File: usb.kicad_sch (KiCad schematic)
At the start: 5 parts, among them U7 USBLC6-2P6

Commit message: added diode
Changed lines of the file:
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@@
 		(color 0 0 0 0)
 	)
+	(junction
+		(at 27.94 111.76)
+		(diameter 0)
+		(color 0 0 0 0)
+	)
 	(wire
 		(pts
@@
 	(wire
 		(pts
+			(xy 27.94 111.76) (xy 27.94 113.03)
+		)
+		(stroke
+			(width 0)
+			(type default)
+		)
+	)
+	(wire
+		(pts
 			(xy 39.37 106.68) (xy 39.37 111.76)
 		)
@@
 	(wire
 		(pts
+			(xy 24.13 111.76) (xy 27.94 111.76)
+		)
+		(stroke
+			(width 0)
+			(type default)
+		)
+	)
+	(wire
+		(pts
 			(xy 27.94 68.58) (xy 31.75 68.58)
 		)
@@
 	(wire
 		(pts
-			(xy 27.94 106.68) (xy 27.94 113.03)
+			(xy 27.94 106.68) (xy 27.94 111.76)
 		)
 		(stroke
@@
 			)
 		)
+	)
+	(symbol
+		(lib_id "power:PWR_FLAG")
+		(at 24.13 111.76 0)
+		(unit 1)
+		(exclude_from_sim no)
+		(in_bom yes)
+		(on_board yes)
+		(dnp no)
+		(fields_autoplaced yes)
+		(property "Reference" "#FLG02"
+			(at 24.13 109.855 0)
+			(effects
+				(font
+					(size 1.27 1.27)
+				)
+				(hide yes)
+			)
+		)
+		(property "Value" "PWR_FLAG"
+			(at 24.13 106.68 0)
+			(effects
+				(font
+					(size 1.27 1.27)
+				)
+			)
+		)
+		(property "Footprint" ""
+			(at 24.13 111.76 0)
+			(effects
+				(font
+					(size 1.27 1.27)
+				)
+				(hide yes)
+			)
+		)
+		(property "Datasheet" "~"
+			(at 24.13 111.76 0)
+			(effects
+				(font
+					(size 1.27 1.27)
+				)
+				(hide yes)
+			)
+		)
+		(property "Description" "Special symbol for telling ERC where power comes from"
+			(at 24.13 111.76 0)
+			(effects
+				(font
+					(size 1.27 1.27)
+				)
+				(hide yes)
+			)
+		)
+		(pin "1"
+		)
+		(instances
+			(project ""
+				(path "/84b8b555-aaa5-476b-b0f2-2d0f894bf0e6/4cda7d87-7e9e-45c2-9c67-fc3e262886b2"
+					(reference "#FLG02")
+					(unit 1)
+				)
+			)
+		)

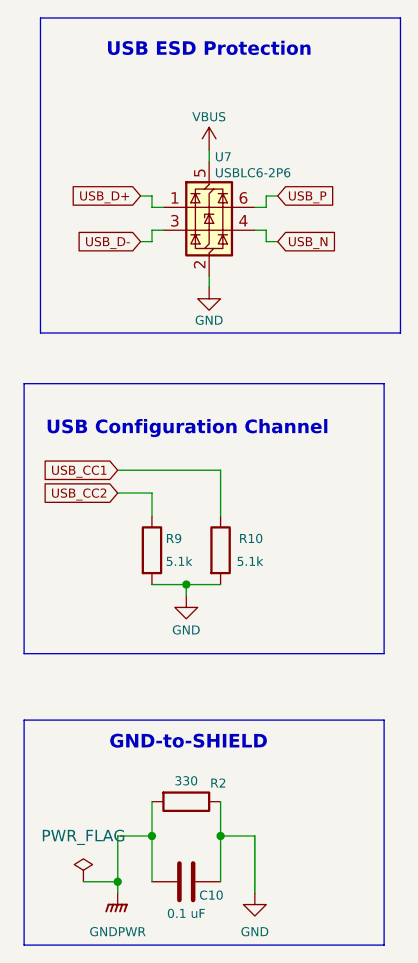
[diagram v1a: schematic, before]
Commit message: separated voltage source labels
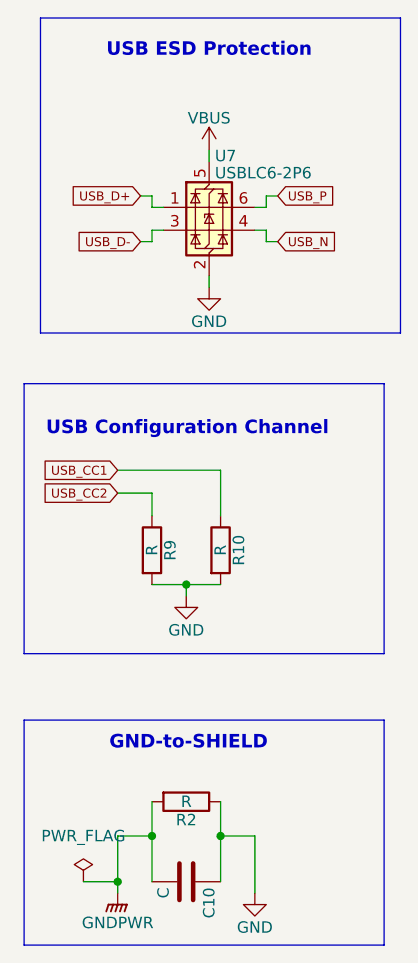
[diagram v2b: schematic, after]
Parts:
- C10: value 0.1 uF -> C
- R10, R9: value 5.1k -> R
- R2: value 330 -> R
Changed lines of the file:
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@@
 		(dnp no)
 		(fields_autoplaced yes)
-		(property "Reference" "#FLG02"
+		(property "Reference" "#FLG2"
 			(at 24.13 109.855 0)
 			(effects
@@
 			(project ""
 				(path "/84b8b555-aaa5-476b-b0f2-2d0f894bf0e6/4cda7d87-7e9e-45c2-9c67-fc3e262886b2"
-					(reference "#FLG02")
+					(reference "#FLG2")
 					(unit 1)
 				)
@@
 		(on_board yes)
 		(dnp no)
-		(property "Reference" "#PWR05"
+		(property "Reference" "#PWR5"
 			(at 27.94 118.11 0)
 			(effects
@@
 		)
 		(property "Value" "GNDPWR"
-			(at 27.94 117.348 0)
-			(effects
-				(font
-					(size 1 1)
+			(at 27.94 116.332 0)
+			(effects
+				(font
+					(size 1.27 1.27)
 				)
 			)
@@
 			(project "apex"
 				(path "/84b8b555-aaa5-476b-b0f2-2d0f894bf0e6/4cda7d87-7e9e-45c2-9c67-fc3e262886b2"
-					(reference "#PWR05")
+					(reference "#PWR5")
 					(unit 1)
 				)
@@
 		(on_board yes)
 		(dnp no)
-		(property "Reference" "#PWR013"
+		(property "Reference" "#PWR13"
 			(at 35.56 86.36 0)
 			(effects
@@
 			(effects
 				(font
-					(size 1 1)
+					(size 1.27 1.27)
 				)
 			)
@@
 			(project "apex"
 				(path "/84b8b555-aaa5-476b-b0f2-2d0f894bf0e6/4cda7d87-7e9e-45c2-9c67-fc3e262886b2"
-					(reference "#PWR013")
+					(reference "#PWR13")
 					(unit 1)
 				)
@@
 		(on_board yes)
 		(dnp no)
-		(property "Reference" "#PWR015"
+		(property "Reference" "#PWR15"
 			(at 43.18 119.38 0)
 			(effects
@@
 		)
 		(property "Value" "GND"
-			(at 43.18 117.348 0)
-			(effects
-				(font
-					(size 1 1)
+			(at 43.18 116.84 0)
+			(effects
+				(font
+					(size 1.27 1.27)
 				)
 			)
@@
 			(project "apex"
 				(path "/84b8b555-aaa5-476b-b0f2-2d0f894bf0e6/4cda7d87-7e9e-45c2-9c67-fc3e262886b2"
-					(reference "#PWR015")
+					(reference "#PWR15")
 					(unit 1)
 				)
@@
 		(dnp no)
 		(property "Reference" "R9"
-			(at 33.274 73.66 0)
-			(effects
-				(font
-					(size 1 1)
-				)
-				(justify left)
-			)
-		)
-		(property "Value" "5.1k"
-			(at 33.274 76.2 0)
-			(effects
-				(font
-					(size 1 1)
-				)
-				(justify left)
+			(at 33.782 74.93 90)
+			(effects
+				(font
+					(size 1.27 1.27)
+				)
+			)
+		)
+		(property "Value" "R"
+			(at 31.75 74.93 90)
+			(effects
+				(font
+					(size 1.27 1.27)
+				)
 			)
 		)
@@
 		(dnp no)
 		(property "Reference" "R2"
-			(at 39.116 100.838 90)
-			(effects
-				(font
-					(size 1 1)
-				)
-			)
-		)
-		(property "Value" "330"
-			(at 35.56 100.584 90)
-			(effects
-				(font
-					(size 1 1)
+			(at 35.56 104.902 90)
+			(effects
+				(font
+					(size 1.27 1.27)
+				)
+			)
+		)
+		(property "Value" "R"
+			(at 35.56 102.87 90)
+			(effects
+				(font
+					(size 1.27 1.27)
 				)
 			)
@@
 		(on_board yes)
 		(dnp no)
-		(property "Reference" "#PWR036"
+		(property "Reference" "#PWR36"
 			(at 38.1 52.07 0)
 			(effects
@@
 		)
 		(property "Value" "GND"
-			(at 38.1 49.403 0)
-			(effects
-				(font
-					(size 1 1)
+			(at 38.1 49.53 0)
+			(effects
+				(font
+					(size 1.27 1.27)
 				)
 			)
@@
 			(project "apex"
 				(path "/84b8b555-aaa5-476b-b0f2-2d0f894bf0e6/4cda7d87-7e9e-45c2-9c67-fc3e262886b2"
-					(reference "#PWR036")
+					(reference "#PWR36")
 					(unit 1)
 				)
@@
 		(on_board yes)
 		(dnp no)
-		(property "Reference" "#PWR035"
+		(property "Reference" "#PWR35"
 			(at 38.1 34.29 0)
 			(effects
@@
 		)
 		(property "Value" "VBUS"
-			(at 38.1 26.797 0)
-			(effects
-				(font
-					(size 1 1)
+			(at 38.1 26.924 0)
+			(effects
+				(font
+					(size 1.27 1.27)
 				)
 			)
@@
 			(project "apex"
 				(path "/84b8b555-aaa5-476b-b0f2-2d0f894bf0e6/4cda7d87-7e9e-45c2-9c67-fc3e262886b2"
-					(reference "#PWR035")
+					(reference "#PWR35")
 					(unit 1)
 				)
@@
 		(dnp no)
 		(property "Reference" "C10"
-			(at 38.354 113.284 90)
-			(effects
-				(font
-					(size 1 1)
-				)
-			)
-		)
-		(property "Value" "0.1 uF"
-			(at 35.56 115.316 90)
-			(effects
-				(font
-					(size 1 1)
-				)
+			(at 38.1 112.395 0)
+			(effects
+				(font
+					(size 1.27 1.27)
+				)
+				(justify left)
+			)
+		)
+		(property "Value" "C"
+			(at 33.02 112.395 0)
+			(effects
+				(font
+					(size 1.27 1.27)
+				)
+				(justify left)
 			)
 		)
@@
 		(dnp no)
 		(property "Reference" "U7"
-			(at 38.735 31.242 0)
-			(effects
-				(font
-					(size 1 1)
+			(at 38.735 31.115 0)
+			(effects
+				(font
+					(size 1.27 1.27)
 				)
 				(justify left)
@@
 			(effects
 				(font
-					(size 1 1)
+					(size 1.27 1.27)
 				)
 				(justify left)
@@
 		(dnp no)
 		(property "Reference" "R10"
-			(at 41.402 73.66 0)
-			(effects
-				(font
-					(size 1 1)
-				)
-				(justify left)
-			)
-		)
-		(property "Value" "5.1k"
-			(at 41.148 76.2 0)
-			(effects
-				(font
-					(size 1 1)
-				)
-				(justify left)
-			)
-		)
+			(at 41.402 74.93 90)
+			(effects
+				(font
+					(size 1.27 1.27)
+				)
+			)
+		)
+		(property "Value" "R"
+			(at 39.37 74.93 90)
+			(effects
+				(font
+					(size 1.27 1.27)
+				)
+			)
+		)
